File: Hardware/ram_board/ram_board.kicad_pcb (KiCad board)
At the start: 2 copper layers, 80.8 x 60.1 mm, 12 parts, among them J1 Conn_01x40, U1 74LS00, U2 28C256, U3 IDT71256SA15

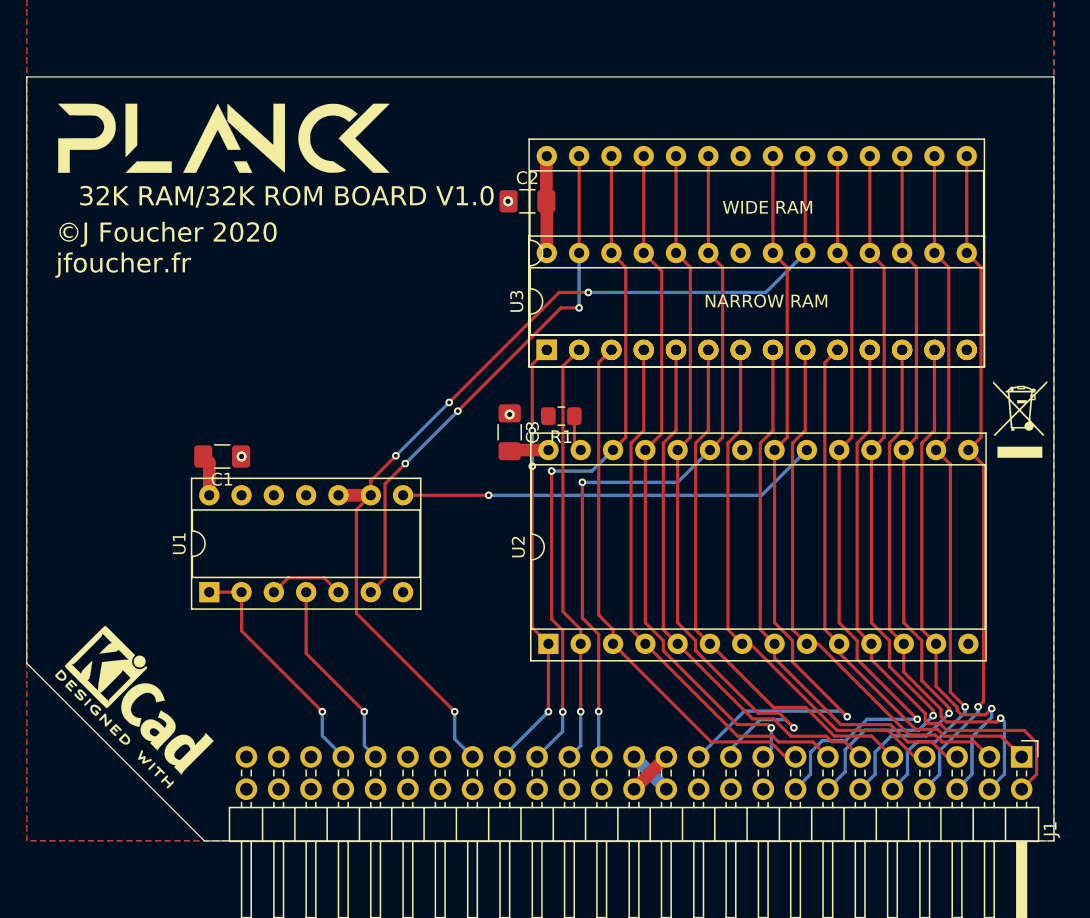
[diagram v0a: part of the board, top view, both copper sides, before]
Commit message: 512K RAM board
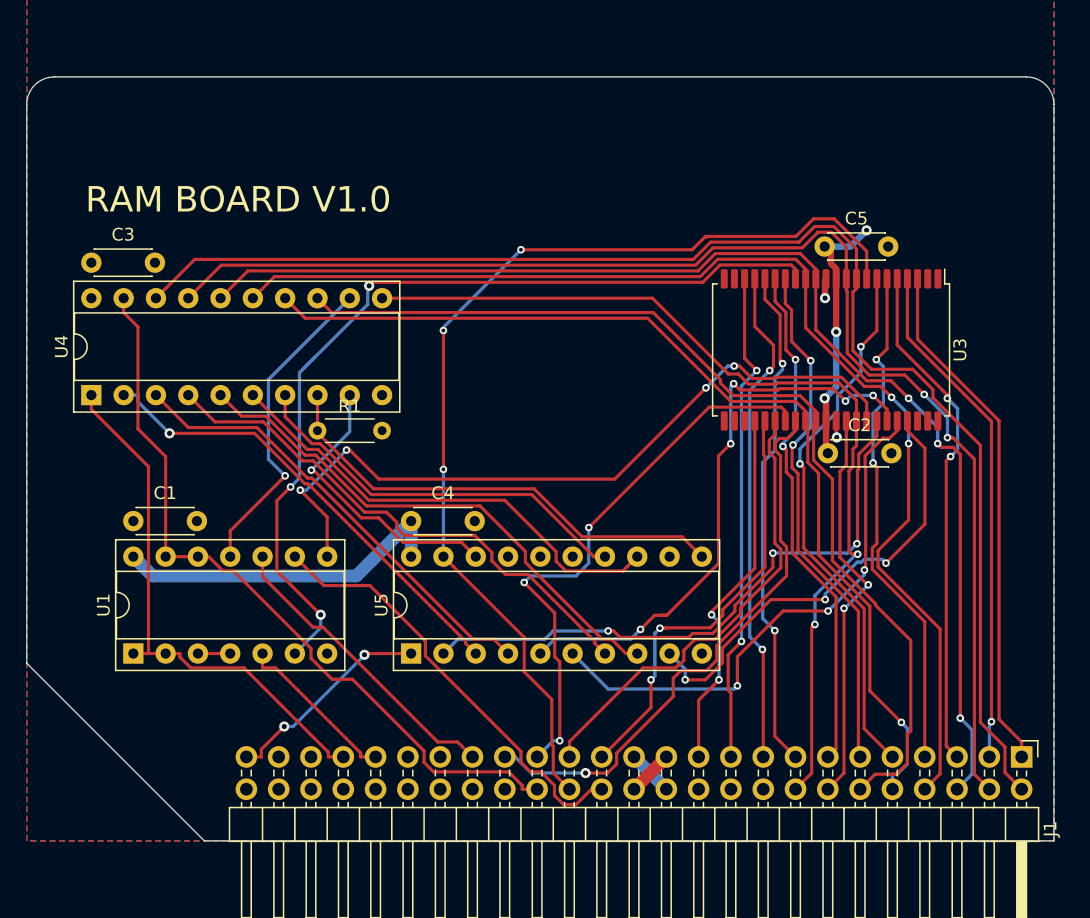
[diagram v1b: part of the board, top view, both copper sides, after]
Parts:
- removed G***: LOGO, logo:logo
- removed REF**: WEEE-Logo_4.2x6mm_SilkScreen, Symbol:WEEE-Logo_4.2x6mm_SilkScreen
- removed REF**: KiCad-Logo2_5mm_SilkScreen, Symbol:KiCad-Logo2_5mm_SilkScreen
- removed U2: 28C256, Package_DIP:DIP-28_W15.24mm_Socket
- removed WIDE RAM: DIP-28_W15.24mm_Socket, Package_DIP:DIP-28_W15.24mm_Socket
- added C4: C_Small, Capacitor_THT:C_Disc_D4.3mm_W1.9mm_P5.00mm, F.Cu at (30.2, -25.1)
- added C5: C_Small, Capacitor_THT:C_Disc_D4.3mm_W1.9mm_P5.00mm, F.Cu at (62.7, -46.7)
- added U4: 74LS245, Package_DIP:DIP-20_W7.62mm_Socket, F.Cu at (5.08, -35.1)
- added U5: 74LS273, Package_DIP:DIP-20_W7.62mm_Socket, F.Cu at (30.2, -14.7)
- C1, C2, C3: footprint Capacitor_SMD:C_1206_3216Metric_Pad1.42x1.75mm_HandSolder -> Capacitor_THT:C_Disc_D4.3mm_W1.9mm_P5.00mm
- R1: footprint Resistor_SMD:R_0805_2012Metric_Pad1.15x1.40mm_HandSolder -> Resistor_THT:R_Axial_DIN0204_L3.6mm_D1.6mm_P5.08mm_Horizontal
- U3: value IDT71256SA15 -> IS61C5128AL-10TLI; footprint Package_DIP:DIP-28_W7.62mm_Socket -> Package_SO:TSOP-II-44_10.16x18.41mm_P0.8mm
- moved C3 35.5 mm to (5.08, -45.5), turned to 0 degrees
- moved C2 30.8 mm to (63.0, -30.5)
- moved U3 22.4 mm to (63.2, -38.6), turned to 270 degrees
- moved R1 19.2 mm to (22.9, -32.3), turned to 0 degrees
- moved C1 8.64 mm to (8.38, -25.1), turned to 0 degrees
- moved U1 7.68 mm to (8.38, -14.7)
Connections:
- net EX6 renamed LED1
- net EX7 renamed LED2
- net EX8 renamed LED3
- net EX9 renamed LED4
- net IRQ renamed ~IRQ~
- net IRQ0 renamed ~SLOT_IRQ~
- net IRQ3 renamed CLK_12M
- net NMI renamed ~NMI~
- net RW renamed R~W~
- C1 pad 1: GND -> +5V
- C1 pad 2: +5V -> GND
- C2 pad 1: GND -> +5V
- C2 pad 2: +5V -> GND
- C3 pad 1: GND -> +5V
- C3 pad 2: +5V -> GND
- J1 pad 22: EX2 -> ~SLOW~
- J1 pad 28: EX3 -> ~SSEL~
- J1 pad 30: EX4 -> ~INH~
- J1 pad 32: EX5 -> ~SLOT_SEL~
- J1 pad 44: IRQ2 -> EX2
- J1 pad 46: IRQ1 -> EX3
- J1 pad 49: RESET -> ~RESET~
- R1 pad 2: +5V -> GND
- U1 pad 12: GND -> ~SLOT_SEL~
- U1 pad 13: GND -> ~SLOT_SEL~
- U1 pad 4: CLK -> Net-(U1-Pad3)
- U1 pad 5: Net-(U1-Pad3) -> CLK
- U1 pad 9: A15 -> ~SSEL~
- U3 pad 1: A14 -> Net-(U3-Pad1)
- U3 pad 10: A0 -> D1
- U3 pad 11: D0 -> +5V
- U3 pad 12: D1 -> GND
- U3 pad 14: GND -> D3
- U3 pad 15: D3 -> Net-(U1-Pad6)
- U3 pad 16: D4 -> A5
- U3 pad 17: D5 -> A6
- U3 pad 18: D6 -> A7
- U3 pad 19: D7 -> A8
- U3 pad 2: A12 -> Net-(U3-Pad2)
- U3 pad 20: A15 -> A9
- U3 pad 21: A10 -> Net-(U3-Pad21)
- U3 pad 22: GND -> Net-(U3-Pad22)
- U3 pad 23: A11 -> Net-(U3-Pad23)
- U3 pad 24: A9 -> Net-(U3-Pad24)
- U3 pad 25: A8 -> Net-(U3-Pad25)
- U3 pad 26: A13 -> A10
- U3 pad 27: Net-(U1-Pad6) -> A11
- U3 pad 28: +5V -> A12
- U3 pad 3: A7 -> A0
- U3 pad 4: A6 -> A1
- U3 pad 5: A5 -> A2
- U3 pad 6: A4 -> A3
- U3 pad 7: A3 -> A4
- U3 pad 8: A2 -> ~INH~
- U3 pad 9: A1 -> D0
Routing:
- net ~INH~: track 0.00 -> 80.5 mm, vias 0 -> 3
- net D0: track 45.4 -> 108.1 mm
- net D1: track 42.1 -> 103.6 mm, vias 1 -> 2
- net ~SLOT_SEL~: track 0.00 -> 59.6 mm
- net D2: track 40.5 -> 96.9 mm, vias 1 -> 3
- net A15: track 77.7 -> 24.0 mm, vias 4 -> 0
- net Net-(U3-Pad38): track 0.00 -> 48.4 mm, vias 0 -> 3
- net Net-(U3-Pad39): track 0.00 -> 46.4 mm, vias 0 -> 5
- net Net-(U3-Pad40): track 0.00 -> 42.7 mm, vias 0 -> 3
- net Net-(U4-Pad4): track 0.00 -> 41.9 mm
- net Net-(U4-Pad5): track 0.00 -> 41.7 mm
- net D3: track 53.1 -> 93.6 mm, vias 1 -> 2
- net Net-(U4-Pad6): track 0.00 -> 36.9 mm
- net Net-(U4-Pad2): track 0.00 -> 36.5 mm, vias 0 -> 1
- net Net-(U3-Pad41): track 0.00 -> 36.4 mm, vias 0 -> 3
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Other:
- outline, holes or cut-outs redrawn
- rule trace_min: 0.2 -> 0.154
- rule via_min_size: 0.4 -> 0.6
- board text added: "RAM BOARD V1.0"
- board text removed: "32K RAM/32K ROM BOARD V1.0"
- board text removed: "NARROW RAM"
- board text removed: "©J Foucher 2020 jfoucher.fr"

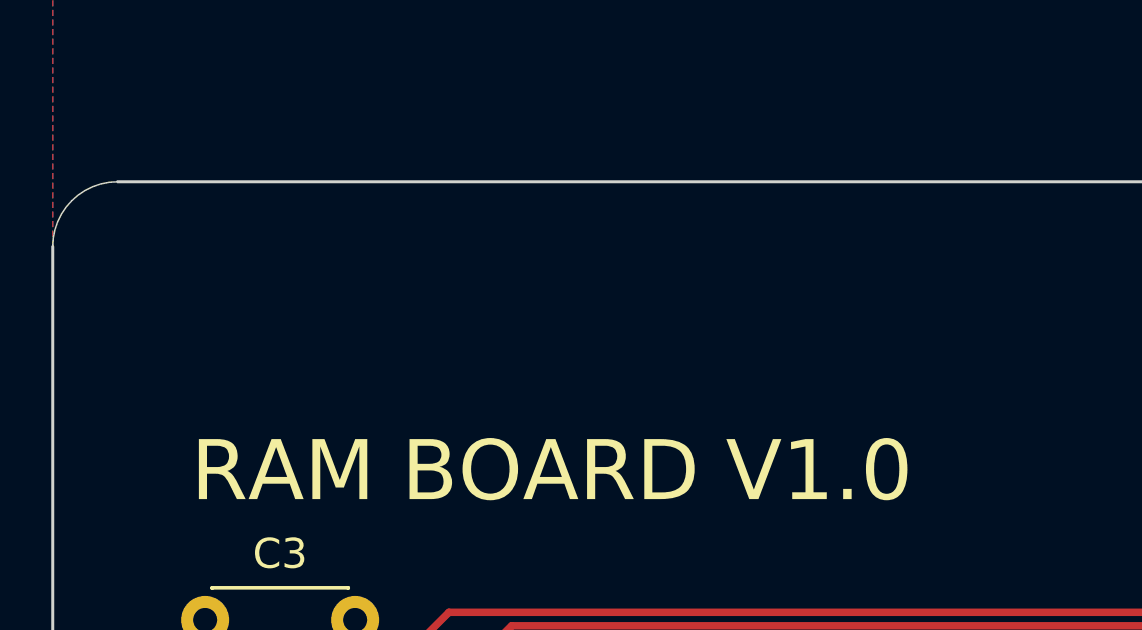
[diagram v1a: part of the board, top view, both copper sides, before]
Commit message: Add ram board gerbers
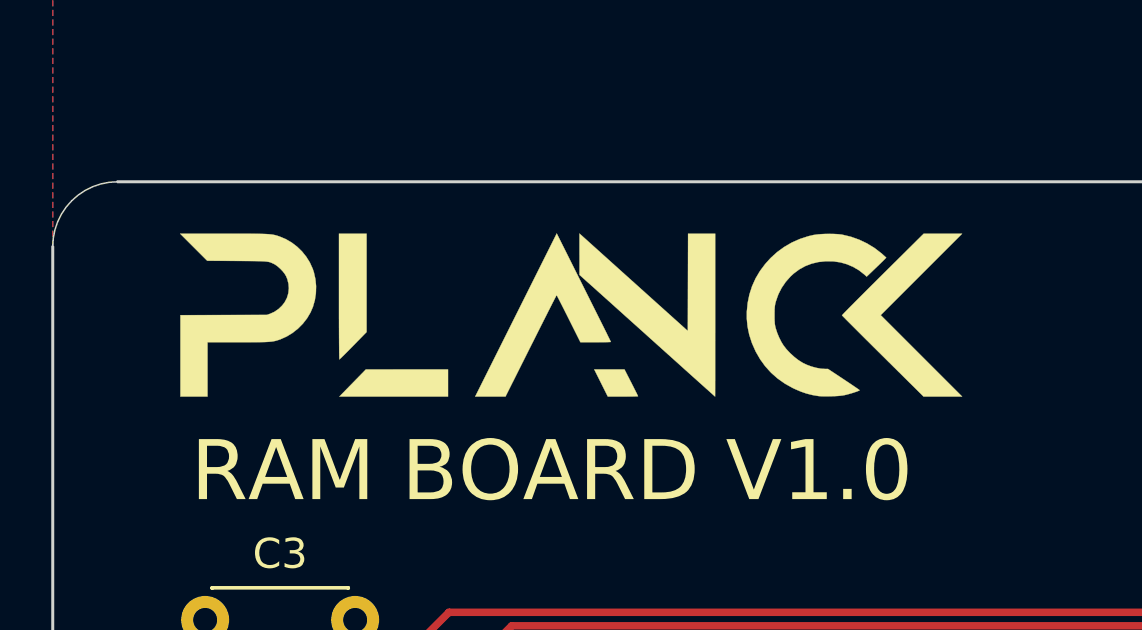
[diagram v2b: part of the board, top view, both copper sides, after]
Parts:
- added G***: LOGO, Logo:logo, B.Cu at (64.0, -56.1)
- added G***: LOGO, Logo:logo, F.Cu at (17.3, -55.6)
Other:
- rule pad_to_mask_clearance: 0.05 -> 0

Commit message: Add banked RAM board
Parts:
- removed R1: R_Small, Resistor_THT:R_Axial_DIN0204_L3.6mm_D1.6mm_P5.08mm_Horizontal
- removed U4: 74LS245, Package_DIP:DIP-20_W7.62mm_Socket
- added C6: 100n, Capacitor_THT:C_Disc_D4.3mm_W1.9mm_P5.00mm, F.Cu at (166.9, 91.9)
- added OSHW: OSHW-Logo2_7.3x6mm_SilkScreen, Symbol:OSHW-Logo2_7.3x6mm_SilkScreen, F.Cu at (113.2, 99.1)
- added REF**: KiCad-Logo2_5mm_SilkScreen, Symbol:KiCad-Logo2_5mm_SilkScreen, F.Cu at (117.6, 128.5)
- added U2: 74HC04, Package_DIP:DIP-14_W7.62mm_Socket, F.Cu at (119.9, 107.3)
- C1, C2, C3, C4: value C_Small -> 100n
- C5: value C_Small -> 10u; footprint Capacitor_THT:C_Disc_D4.3mm_W1.9mm_P5.00mm -> Capacitor_THT:C_Radial_D5.0mm_H11.0mm_P2.00mm
- U1: value 74LS00 -> 74HC00
- U5: value 74LS273 -> 74HC273
- moved C3 185.8 mm to (124.5, 96.8), turned to 180 degrees
- moved C4 180.1 mm to (146.6, 112.3), turned to 180 degrees
- moved C1 180.0 mm to (124.7, 112.3), turned to 180 degrees
- moved C2 179.7 mm to (171.3, 112.9), turned to 90 degrees
- moved C5 179.6 mm to (151.3, 109.5)
- moved U5 177.0 mm to (141.6, 122.8)
- moved U1 177.0 mm to (119.8, 122.8)
- moved J1 176.0 mm to (186.8, 132.0)
- moved LOGO 176.0 mm to (125.9, 82.9)
- moved LOGO2 176.0 mm to (172.6, 82.4)
- moved U3 176.0 mm to (171.8, 99.9)
- renumbered G*** to LOGO, G*** to LOGO2
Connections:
- net Net-(U1-Pad6) renamed /~{WE}
- net Net-(U1-Pad8) renamed /~{OE}
- net ~IRQ~ renamed ~{IRQ}
- net ~NMI~ renamed ~{NMI}
- net ~RESET~ renamed ~{RESET}
- net ~SLOT_IRQ~ renamed ~{SLOT_IRQ}
- net ~SLOW~ renamed ~{SLOW}
- C1 pad 1: +5V -> GND
- C1 pad 2: GND -> +5V
- C2 pad 1: +5V -> GND
- C2 pad 2: GND -> +5V
- C3 pad 1: +5V -> GND
- C3 pad 2: GND -> +5V
- C4 pad 1: +5V -> GND
- C4 pad 2: GND -> +5V
- J1 pad 28: ~SSEL~ -> ~{SSEL}
- J1 pad 30: ~INH~ -> ~{INH}
- J1 pad 32: ~SLOT_SEL~ -> ~{SLOT_SEL}
- J1 pad 43: R~W~ -> R~{W}
- U1 pad 1: R~W~ -> Net-(U1-Pad1)
- U1 pad 12: ~SLOT_SEL~ -> ~{SLOT_SEL}
- U1 pad 13: ~SLOT_SEL~ -> CLK
- U1 pad 2: R~W~ -> /~{CE}
- U1 pad 3: Net-(U1-Pad3) -> ~{INH}
- U1 pad 4: Net-(U1-Pad3) -> Net-(U1-Pad4)
- U1 pad 9: ~SSEL~ -> Net-(U1-Pad9)
- U3 pad 1: Net-(U3-Pad1) -> unconnected-(U3-Pad1)
- U3 pad 2: Net-(U3-Pad2) -> unconnected-(U3-Pad2)
- U3 pad 21: Net-(U3-Pad21) -> unconnected-(U3-Pad21)
- U3 pad 22: Net-(U3-Pad22) -> unconnected-(U3-Pad22)
- U3 pad 23: Net-(U3-Pad23) -> unconnected-(U3-Pad23)
- U3 pad 24: Net-(U3-Pad24) -> unconnected-(U3-Pad24)
- U3 pad 25: Net-(U3-Pad25) -> unconnected-(U3-Pad25)
- U3 pad 30: A14 -> /RA14
- U3 pad 38: Net-(U3-Pad38) -> /RA15
- U3 pad 39: Net-(U3-Pad39) -> /RA16
- U3 pad 40: Net-(U3-Pad40) -> /RA17
- U3 pad 41: Net-(U3-Pad41) -> /RA18
- U3 pad 42: Net-(U3-Pad42) -> unconnected-(U3-Pad42)
- U3 pad 43: Net-(U3-Pad43) -> unconnected-(U3-Pad43)
- U3 pad 44: Net-(U3-Pad44) -> unconnected-(U3-Pad44)
- U3 pad 8: ~INH~ -> /~{CE}
- U5 pad 11: Net-(R1-Pad1) -> Net-(U1-Pad11)
- U5 pad 12: Net-(U5-Pad12) -> /RA18
- U5 pad 13: Net-(U4-Pad6) -> D4
- U5 pad 14: Net-(U4-Pad7) -> D5
- U5 pad 15: Net-(U5-Pad15) -> unconnected-(U5-Pad15)
- U5 pad 16: Net-(U5-Pad16) -> unconnected-(U5-Pad16)
- U5 pad 17: GND -> D6
- U5 pad 18: Net-(U4-Pad9) -> D7
- U5 pad 19: ~INH~ -> Net-(U2-Pad11)
- U5 pad 2: Net-(U3-Pad38) -> /RA14
- U5 pad 3: Net-(U4-Pad2) -> D0
- U5 pad 4: Net-(U4-Pad3) -> D1
- U5 pad 5: Net-(U3-Pad39) -> /RA15
- U5 pad 6: Net-(U3-Pad40) -> /RA16
- U5 pad 7: Net-(U4-Pad4) -> D2
- U5 pad 8: Net-(U4-Pad5) -> D3
- U5 pad 9: Net-(U3-Pad41) -> /RA17
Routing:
- net ~INH~: track 80.5 -> 0.00 mm, vias 3 -> 0
- net /~{CE}: track 0.00 -> 80.4 mm, vias 0 -> 3
- net ~SLOT_SEL~: track 59.6 -> 0.00 mm
- net Net-(U3-Pad38): track 48.4 -> 0.00 mm, vias 3 -> 0
- net Net-(U3-Pad39): track 46.4 -> 0.00 mm, vias 5 -> 0
- net Net-(U3-Pad40): track 42.7 -> 0.00 mm, vias 3 -> 0
- net R~W~: track 42.4 -> 0.00 mm
- net Net-(U4-Pad4): track 41.9 -> 0.00 mm
- net Net-(U4-Pad5): track 41.7 -> 0.00 mm
- net +5V: track 51.5 -> 10.5 mm, vias 3 -> 0
- net /RA14: track 0.00 -> 40.3 mm, vias 0 -> 1
- net /RA15: track 0.00 -> 38.2 mm, vias 0 -> 1
- net Net-(R1-Pad1): track 37.2 -> 0.00 mm
- net ~{SLOT_SEL}: track 0.00 -> 37.2 mm, vias 0 -> 1
- net R~{W}: track 0.00 -> 37.1 mm, vias 0 -> 2
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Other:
- net class Default removed
- board text added: "RAM BOARD ${VERSION}"
- board text removed: "RAM BOARD V1.0"

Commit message: Add JLC text
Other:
- board text added: "JLCJLCJLCJLC"
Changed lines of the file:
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@@
     (effects (font (size 2 2) (thickness 0.3)) (justify mirror))
+  )
+  (gr_text "JLCJLCJLCJLC" (at 171.069 96.901) (layer "F.SilkS")
+    (effects (font (size 1 1) (thickness 0.15)))
   )
   (gr_text "RAM BOARD ${VERSION}" (at 125.222 88.138) (layer "F.SilkS")

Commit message: Add RAM board + some VGA things
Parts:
- added C7: 100n, Capacitor_THT:C_Disc_D4.3mm_W1.9mm_P5.00mm, F.Cu at (145.9, 84.8)
- added U4: 74LS32, Package_DIP:DIP-14_W7.62mm_Socket, F.Cu at (144.9, 88.5)
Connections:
- U1 pad 11: Net-(U1-Pad11) -> unconnected-(U1-Pad11)
- U1 pad 12: ~{SLOT_SEL} -> GND
- U1 pad 13: CLK -> GND
- U1 pad 2: /~{CE} -> Net-(U5-Q7)
- U2 pad 11: Net-(U2-Pad11) -> Net-(U5-Q7)
- U5 pad 11: Net-(U1-Pad11) -> Net-(U5-Cp)
- U5 pad 19: Net-(U2-Pad11) -> Net-(U5-Q7)
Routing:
- net Net-(U5-Q7): track 0.00 -> 55.5 mm, vias 0 -> 2
- net Net-(U5-Cp): track 0.00 -> 40.4 mm, vias 0 -> 2
- net Net-(U1-Pad11): track 40.4 -> 0.00 mm, vias 2 -> 0
- net /~{CE}: track 80.4 -> 52.2 mm, vias 3 -> 2
- net Net-(U2-Pad11): track 25.9 -> 0.00 mm, vias 2 -> 0

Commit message: fix RAM board ERC and DRC
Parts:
- U4: value 74LS32 -> 74HC02
- moved U4 15.6 mm to (158.5, 96.1), turned to -90 degrees
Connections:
- U4 pad 1: ~{SLOT_SEL} -> Net-(U5-Cp)
- U4 pad 10: GND -> unconnected-(U4-Pad10)
- U4 pad 11: unconnected-(U4-Pad11) -> GND
- U4 pad 13: GND -> unconnected-(U4-Pad13)
- U4 pad 2: CLK -> ~{SLOT_SEL}
- U4 pad 3: Net-(U5-Cp) -> CLK
- U4 pad 4: GND -> unconnected-(U4-Pad4)
- U4 pad 6: unconnected-(U4-Pad6) -> GND
- U4 pad 8: unconnected-(U4-Pad8) -> GND
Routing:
- net CLK: track 23.9 -> 52.0 mm, vias 2 -> 4
- net Net-(U5-Cp): track 40.4 -> 21.7 mm
- net ~{SLOT_SEL}: track 37.2 -> 45.7 mm, vias 1 -> 3
- net /~{OE}: track 64.5 -> 58.5 mm
- net +5V: track 10.5 -> 14.1 mm
- net /~{WE}: track 65.9 -> 64.4 mm
- net GND: track 17.7 -> 18.6 mm
